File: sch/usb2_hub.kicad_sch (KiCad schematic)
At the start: 49 parts, among them J10 USB_A, J6 USB_A, J7 USB_A, J8 USB_B, J9 USB_A, Q2 2N7002P, U5 MIC2026-1BM, U6 MIC2026-1BM, U7 USB2514B_Bi, Y2 24MHz

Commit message: update label for easy routing differential pair
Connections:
- net H_U_P: now reaches J8.2 (D-), U7.30 (USBDM_UP)
- net H_U_N: now reaches J8.3 (D+), U7.31 (USBDP_UP)
- net H_D1_N: now reaches J6.2 (D-), U7.1 (USBDM_DN1/PRT_DIS_M1)
- net H_D1_P: now reaches J6.3 (D+), U7.2 (USBDP_DN1/PRT_DIS_P1)
- net H_D2_N: now reaches J7.2 (D-), U7.3 (USBDM_DN2/PRT_DIS_M2)
- net H_D2_P: now reaches J7.3 (D+), U7.4 (USBDP_DN2/PRT_DIS_P2)
- net H_D3_N: now reaches J9.2 (D-), U7.6 (USBDM_DN3/PRT_DIS_M3)
- net H_D3_P: now reaches J9.3 (D+), U7.7 (USBDP_DN3/PRT_DIS_P3)
- net H_D4_N: now reaches J10.2 (D-), U7.8 (USBDM_DN4/PRT_DIS_M4)
- net H_D4_P: now reaches J10.3 (D+), U7.9 (USBDP_DN4/PRT_DIS_P4)
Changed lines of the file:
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@@
     (stroke (width 0) (type default) (color 0 0 0 0))
   )
-  (wire (pts (xy 200.66 119.38) (xy 179.07 119.38))
+  (wire (pts (xy 200.66 118.11) (xy 181.61 118.11))
     (stroke (width 0) (type default) (color 0 0 0 0))
   )
@@
     (stroke (width 0) (type default) (color 0 0 0 0))
   )
+  (wire (pts (xy 181.61 106.68) (xy 179.07 106.68))
+    (stroke (width 0) (type default) (color 0 0 0 0))
+  )
   (wire (pts (xy 121.92 72.39) (xy 132.08 72.39))
     (stroke (width 0) (type default) (color 0 0 0 0))
@@
     (stroke (width 0) (type default) (color 0 0 0 0))
   )
-  (wire (pts (xy 200.66 119.38) (xy 200.66 124.46))
+  (wire (pts (xy 200.66 118.11) (xy 200.66 124.46))
     (stroke (width 0) (type default) (color 0 0 0 0))
   )
@@
     (stroke (width 0) (type default) (color 0 0 0 0))
   )
-  (wire (pts (xy 179.07 132.08) (xy 198.12 132.08))
+  (wire (pts (xy 181.61 130.81) (xy 198.12 130.81))
     (stroke (width 0) (type default) (color 0 0 0 0))
   )
@@
     (stroke (width 0) (type default) (color 0 0 0 0))
   )
+  (wire (pts (xy 181.61 105.41) (xy 181.61 106.68))
+    (stroke (width 0) (type default) (color 0 0 0 0))
+  )
   (wire (pts (xy 111.76 168.91) (xy 116.84 168.91))
     (stroke (width 0) (type default) (color 0 0 0 0))
@@
     (stroke (width 0) (type default) (color 0 0 0 0))
   )
+  (wire (pts (xy 181.61 118.11) (xy 181.61 119.38))
+    (stroke (width 0) (type default) (color 0 0 0 0))
+  )
   (bus (pts (xy 190.5 124.46) (xy 190.5 137.16))
     (stroke (width 0) (type default) (color 0 0 0 0))
@@
     (stroke (width 0) (type default) (color 0 0 0 0))
   )
+  (wire (pts (xy 181.61 130.81) (xy 181.61 132.08))
+    (stroke (width 0) (type default) (color 0 0 0 0))
+  )
   (bus (pts (xy 162.56 26.67) (xy 162.56 34.29))
     (stroke (width 0) (type default) (color 0 0 0 0))
@@
     (stroke (width 0) (type default) (color 0 0 0 0))
   )
+  (wire (pts (xy 181.61 119.38) (xy 179.07 119.38))
+    (stroke (width 0) (type default) (color 0 0 0 0))
+  )
   (wire (pts (xy 260.35 102.87) (xy 260.35 104.14))
     (stroke (width 0) (type default) (color 0 0 0 0))
@@
     (stroke (width 0) (type default) (color 0 0 0 0))
   )
-  (wire (pts (xy 198.12 132.08) (xy 198.12 151.13))
-    (stroke (width 0) (type default) (color 0 0 0 0))
-  )
-  (wire (pts (xy 179.07 93.98) (xy 203.2 93.98))
+  (wire (pts (xy 198.12 130.81) (xy 198.12 151.13))
+    (stroke (width 0) (type default) (color 0 0 0 0))
+  )
+  (wire (pts (xy 181.61 92.71) (xy 203.2 92.71))
     (stroke (width 0) (type default) (color 0 0 0 0))
   )
@@
     (stroke (width 0) (type default) (color 0 0 0 0))
   )
-  (wire (pts (xy 203.2 73.66) (xy 203.2 93.98))
+  (wire (pts (xy 203.2 73.66) (xy 203.2 92.71))
     (stroke (width 0) (type default) (color 0 0 0 0))
   )
@@
     (stroke (width 0) (type default) (color 0 0 0 0))
   )
-  (wire (pts (xy 203.2 106.68) (xy 203.2 99.06))
+  (wire (pts (xy 203.2 105.41) (xy 203.2 99.06))
     (stroke (width 0) (type default) (color 0 0 0 0))
   )
@@
     (stroke (width 0) (type default) (color 0 0 0 0))
   )
+  (wire (pts (xy 181.61 93.98) (xy 179.07 93.98))
+    (stroke (width 0) (type default) (color 0 0 0 0))
+  )
   (wire (pts (xy 255.27 92.71) (xy 255.27 93.98))
     (stroke (width 0) (type default) (color 0 0 0 0))
@@
     (stroke (width 0) (type default) (color 0 0 0 0))
   )
+  (wire (pts (xy 181.61 92.71) (xy 181.61 93.98))
+    (stroke (width 0) (type default) (color 0 0 0 0))
+  )
   (wire (pts (xy 246.38 78.74) (xy 246.38 85.09))
     (stroke (width 0) (type default) (color 0 0 0 0))
@@
     (stroke (width 0) (type default) (color 0 0 0 0))
   )
+  (wire (pts (xy 181.61 132.08) (xy 179.07 132.08))
+    (stroke (width 0) (type default) (color 0 0 0 0))
+  )
   (wire (pts (xy 133.35 43.18) (xy 154.94 43.18))
     (stroke (width 0) (type default) (color 0 0 0 0))
@@
     (stroke (width 0) (type default) (color 0 0 0 0))
   )
-  (wire (pts (xy 179.07 106.68) (xy 203.2 106.68))
+  (wire (pts (xy 181.61 105.41) (xy 203.2 105.41))
     (stroke (width 0) (type default) (color 0 0 0 0))
   )
@@
     (effects (font (size 1.27 1.27)) (justify left bottom))
   )
+  (label "H_D1_P" (at 182.88 95.25 0)
+    (effects (font (size 1.27 1.27)) (justify left bottom))
+  )
   (label "V_Ch1" (at 194.31 26.67 0)
     (effects (font (size 1.27 1.27)) (justify left bottom))
@@
     (effects (font (size 1.27 1.27)) (justify right bottom))
   )
+  (label "H_D3_P" (at 182.88 120.65 0)
+    (effects (font (size 1.27 1.27)) (justify left bottom))
+  )
   (label "PRTPWR3" (at 163.83 52.07 0)
     (effects (font (size 1.27 1.27)) (justify left bottom))
@@
     (effects (font (size 1.27 1.27)) (justify left bottom))
   )
+  (label "H_D3_N" (at 181.61 118.11 0)
+    (effects (font (size 1.27 1.27)) (justify left bottom))
+  )
   (label "OCSn2" (at 180.34 114.3 0)
+    (effects (font (size 1.27 1.27)) (justify left bottom))
+  )
+  (label "H_D4_N" (at 181.61 130.81 0)
+    (effects (font (size 1.27 1.27)) (justify left bottom))
+  )
+  (label "H_D2_P" (at 182.88 107.95 0)
     (effects (font (size 1.27 1.27)) (justify left bottom))
   )
@@
     (effects (font (size 1.27 1.27)) (justify right bottom))
   )
+  (label "H_D4_P" (at 182.88 133.35 0)
+    (effects (font (size 1.27 1.27)) (justify left bottom))
+  )
+  (label "H_D2_N" (at 181.61 105.41 0)
+    (effects (font (size 1.27 1.27)) (justify left bottom))
+  )
   (label "RESETn" (at 115.57 106.68 0)
     (effects (font (size 1.27 1.27)) (justify left bottom))
@@
     (effects (font (size 1.27 1.27)) (justify left bottom))
   )
+  (label "H_U_P" (at 115.57 99.06 0)
+    (effects (font (size 1.27 1.27)) (justify left bottom))
+  )
+  (label "H_D1_N" (at 181.61 92.71 0)
+    (effects (font (size 1.27 1.27)) (justify left bottom))
+  )
   (label "PRTPWR2" (at 163.83 29.21 0)
     (effects (font (size 1.27 1.27)) (justify left bottom))
@@
     (effects (font (size 1.27 1.27)) (justify left bottom))
   )
+  (label "H_U_N" (at 115.57 101.6 0)
+    (effects (font (size 1.27 1.27)) (justify left bottom))
+  )

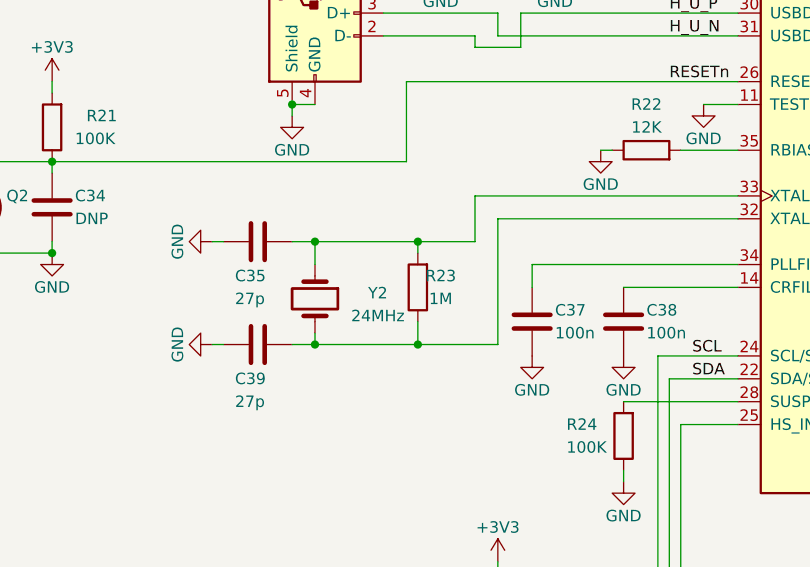
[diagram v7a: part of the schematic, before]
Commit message: layout usb hub
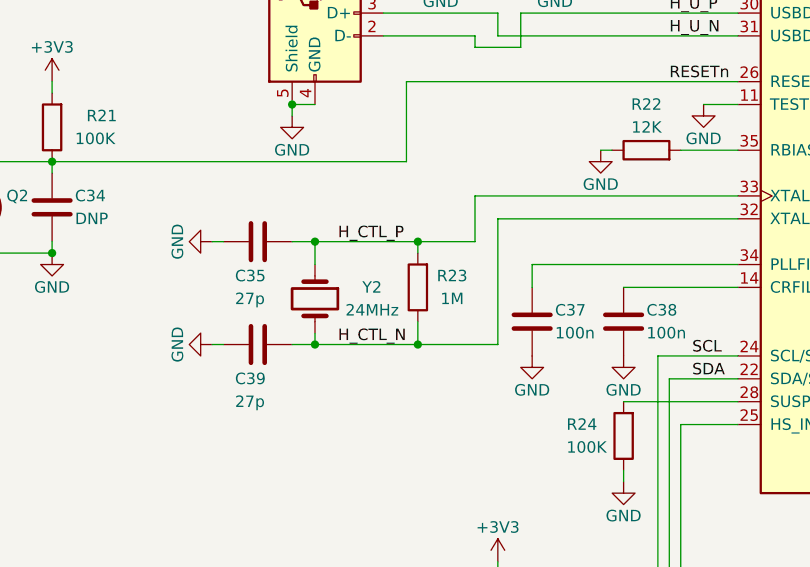
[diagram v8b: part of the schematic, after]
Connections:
- net H_CTL_P: now reaches C35.1, R23.2, U7.33 (XTALIN/CLKIN), Y2.1
- net H_CTL_N: now reaches C39.1, R23.1, U7.32 (XTALOUT), Y2.2
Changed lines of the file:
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@@
+    (effects (font (size 1.27 1.27)) (justify left bottom))
+  )
+  (label "H_CTL_N" (at 78.74 135.89 0)
     (effects (font (size 1.27 1.27)) (justify left bottom))
   )
@@
   )
   (label "H_U_P" (at 115.57 99.06 0)
+    (effects (font (size 1.27 1.27)) (justify left bottom))
+  )
+  (label "H_CTL_P" (at 78.74 124.46 0)
     (effects (font (size 1.27 1.27)) (justify left bottom))
   )
@@
   (symbol (lib_id "Device:Crystal") (at 76.2 130.81 270) (unit 1)
     (in_bom yes) (on_board yes)
-    (property "Reference" "Y2" (id 0) (at 83.185 130.175 90))
-    (property "Value" "24MHz" (id 1) (at 83.185 132.715 90))
+    (property "Reference" "Y2" (id 0) (at 82.55 129.54 90))
+    (property "Value" "24MHz" (id 1) (at 82.55 132.08 90))
     (property "Footprint" "Crystal:Crystal_SMD_5032-2Pin_5.0x3.2mm_HandSoldering" (id 2) (at 76.2 130.81 0)
       (effects (font (size 1.27 1.27)) hide)
@@
   (symbol (lib_id "Device:R") (at 87.63 129.54 180) (unit 1)
     (in_bom yes) (on_board yes)
-    (property "Reference" "R23" (id 0) (at 90.17 128.27 0))
-    (property "Value" "1M" (id 1) (at 90.17 130.81 0))
+    (property "Reference" "R23" (id 0) (at 91.44 128.27 0))
+    (property "Value" "1M" (id 1) (at 91.44 130.81 0))
     (property "Footprint" "Resistor_SMD:R_0603_1608Metric_Pad0.98x0.95mm_HandSolder" (id 2) (at 89.408 129.54 90)
       (effects (font (size 1.27 1.27)) hide)
